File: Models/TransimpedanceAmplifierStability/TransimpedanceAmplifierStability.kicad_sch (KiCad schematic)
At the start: 32 parts

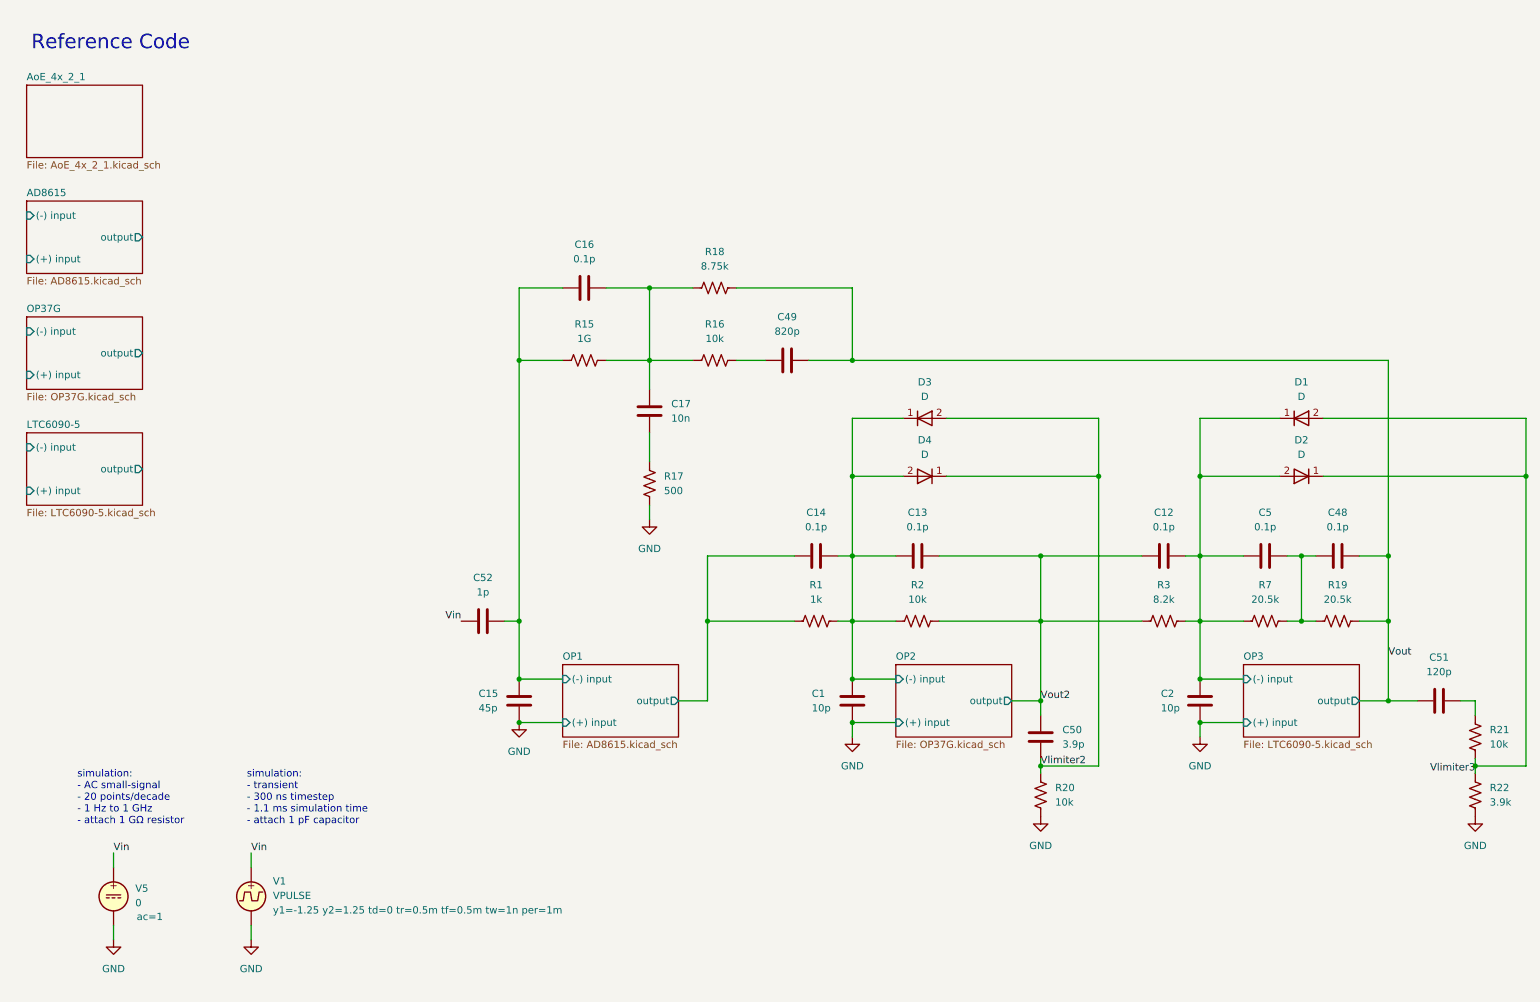
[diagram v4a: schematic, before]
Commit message: Finally came up with a modification to the fast low-noise TIA
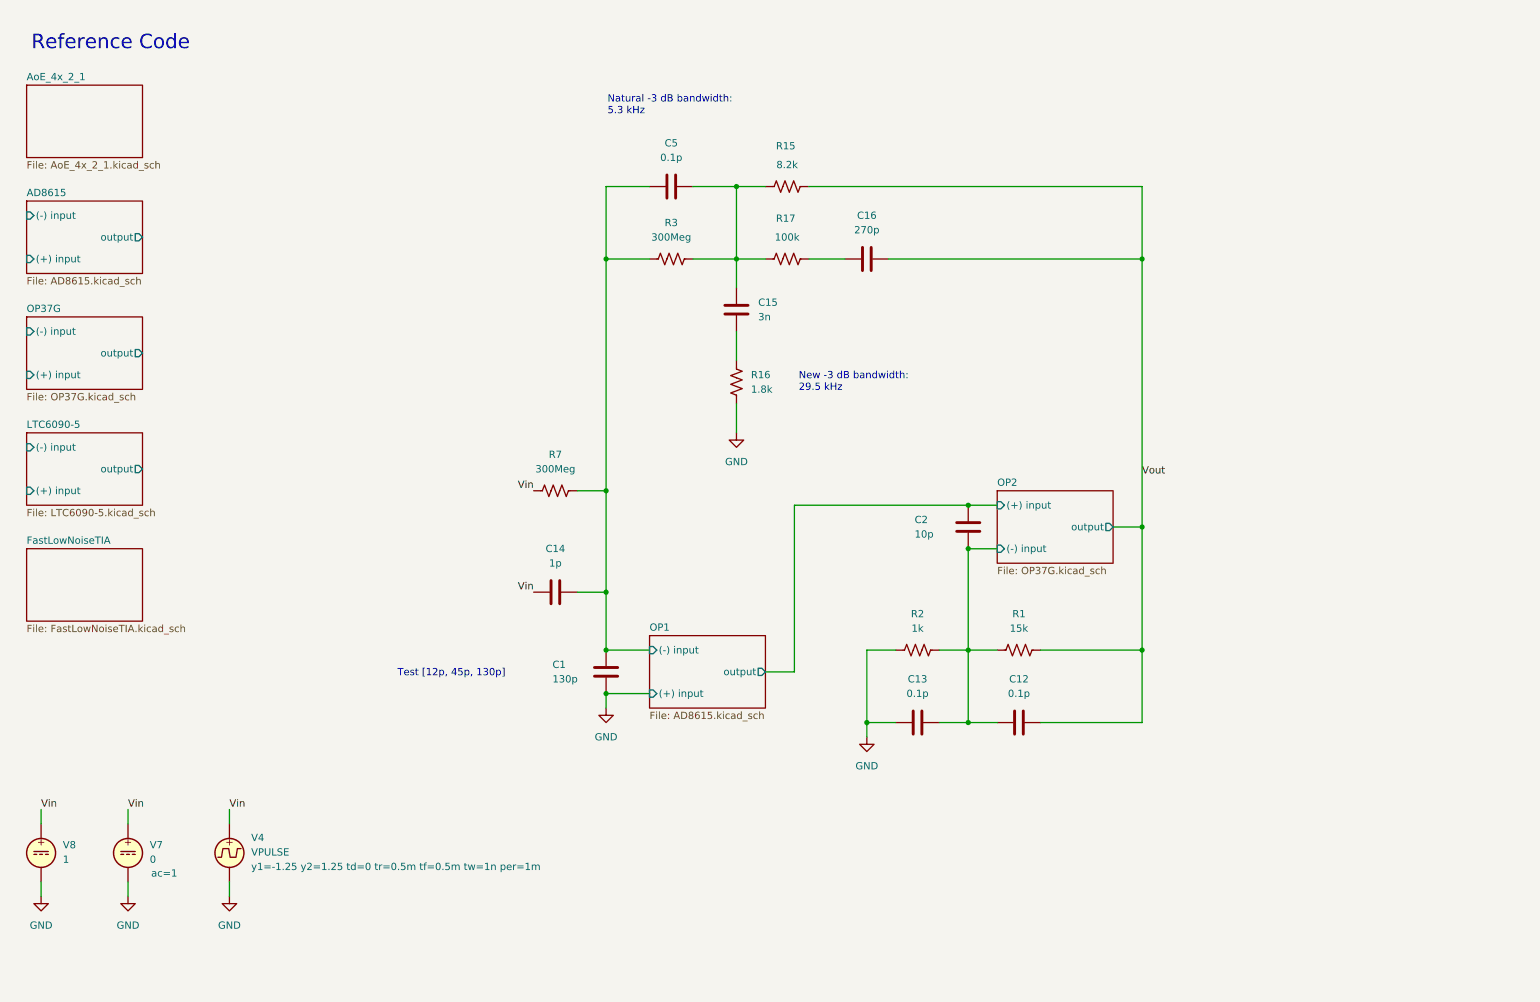
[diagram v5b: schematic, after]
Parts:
- removed C17: 10n, symbol Device:C
- removed C48: 0.1p, symbol Device:C
- removed C49: 820p, symbol Device:C
- removed C50: 3.9p, symbol Device:C
- removed C51: 120p, symbol Device:C
- removed C52: 1p, symbol Device:C
- removed D1, D2, D3, D4: D, symbol Simulation_SPICE:D
- removed R18: 8.75k, symbol Device:R_US
- removed R19: 20.5k, symbol Device:R_US
- removed R20, R21: 10k, symbol Device:R_US
- removed R22: 3.9k, symbol Device:R_US
- removed V1: VPULSE, symbol Simulation_SPICE:VPULSE
- removed V5: 0, symbol Simulation_SPICE:VDC
- added V4: VPULSE, symbol Simulation_SPICE:VPULSE
- added V7: 0, symbol Simulation_SPICE:VDC
- added V8: 1, symbol Simulation_SPICE:VDC
- C1: value 10p -> 130p
- C14: value 0.1p -> 1p
- C15: value 45p -> 3n
- C16: value 0.1p -> 270p
- R1: value 1k -> 15k
- R15: value 1G -> 8.2k
- R16: value 10k -> 1.8k
- R17: value 500 -> 100k
- R2: value 10k -> 1k
- R3: value 8.2k -> 300Meg
- R7: value 20.5k -> 300Meg
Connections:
- net GND: now also C13.1, R16.2, R2.1, V4.2, V7.2, V8.2; no longer C15.2, C2.2, R17.2
- net OP1/(-) input: now also C1.1, C14.2, C5.1, R3.1, R7.2; no longer C15.1, C16.1, R15.1
- net OP1/output: now also C2.1; no longer C14.1, R1.1
- net OP2/(-) input: now also C12.1, C13.2, C2.2, R1.1, R2.2; no longer C1.1, C13.1, C14.2, R1.2, R2.1
- net Vin: now also C14.1, R7.1, V4.1, V7.1, V8.1
- net Vout: now also C12.2, C16.2, R1.2, R15.2
- net at C5.2: now also C15.1, R15.1, R17.1, R3.2; no longer R7.2
- removed net OP3/(-) input: C12.2, C2.1, C5.1, R3.2, R7.1
- removed net Vout2: C12.1, C13.2, R2.2, R3.1
- new net: C16.1, R17.2
- new net: C15.2, R16.1
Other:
- removed sheet OP3
- added sheet FastLowNoiseTIA (FastLowNoiseTIA.kicad_sch)
- note added: "Natural -3 dB bandwidth: 5.3 kHz"
- note added: "New -3 dB bandwidth: 29.5 kHz"
- note added: "Test [12p, 45p, 130p]"
- note removed: "simulation: - AC small-signal - 20 points/decade - 1 Hz to 1 GHz - attach 1 GΩ resistor"
- note removed: "simulation: - transient - 300 ns timestep - 1.1 ms simulation time - attach 1 pF capacitor"
